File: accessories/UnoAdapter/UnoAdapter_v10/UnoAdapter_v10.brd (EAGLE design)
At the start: 71.1 x 85.7 mm, 10 parts, among them IC1 7805, X1 DC21MMX

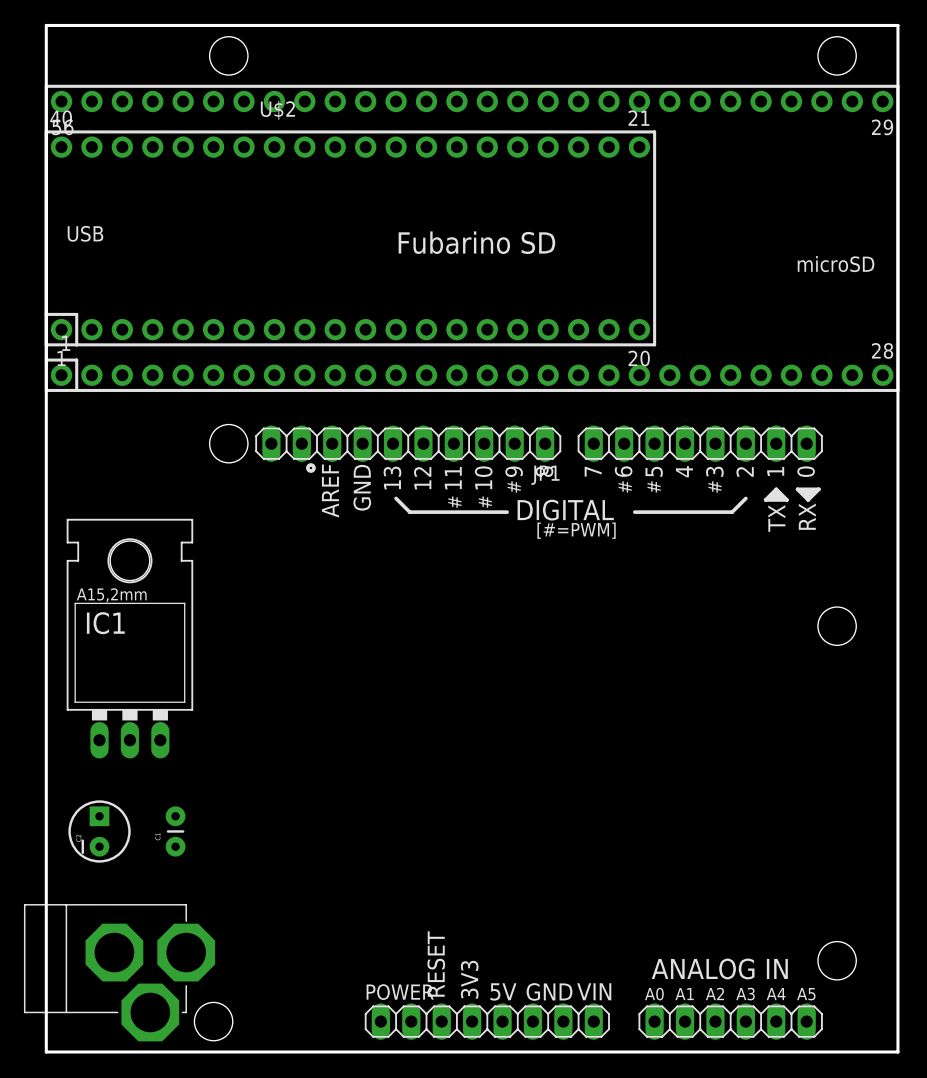
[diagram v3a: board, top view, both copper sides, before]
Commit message: Got some more work done on the board - fixed power issues, added reset/prg switches, moved Fubarinos inside Uno headers.
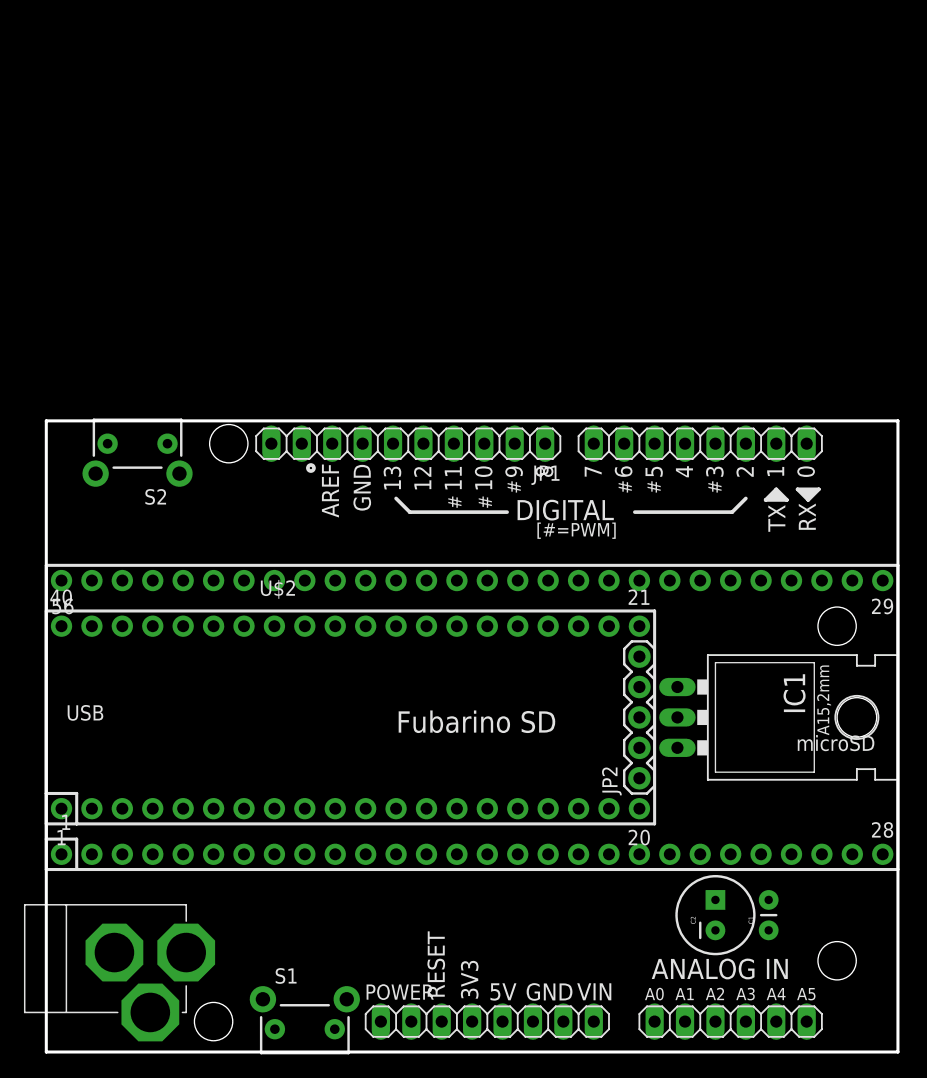
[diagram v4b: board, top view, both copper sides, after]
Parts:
- added JP2: (no value), SparkFun-Connectors:1X05
- added S1, S2: SWITCH-MOMENTARY-2SIDE_EZ, SparkFun-Electromechanical:TACTILE-PTH-SIDEEZ
- C2: value 10uF -> 100uF; device SparkFun-Capacitors:CPOL-RADIAL-10UF-25V -> SparkFun-Capacitors:CPOL-RADIAL-100UF-25V
- moved C2 51.9 mm to (55.9, 11.4)
- moved C1 50.0 mm to (60.3, 10.2)
- moved IC1 49.6 mm to (56.5, 27.9), turned to 270 degrees
- moved U$1 40.0 mm to (35.6, 27.9)
- moved U$2 40.0 mm to (25.4, 27.9)
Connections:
- removed net N$86: U$2.20
- new net N$12: JP2.4
- new net N$2: JP2.2
- new net N$3: JP2.3
- new net PRG: S2.2, U$1.27, U$2.20
- net GND: now also S1.1, S2.1
- net N$28: now also JP2.5; no longer U$1.27
- net RESET: now also JP2.1, S1.2
- net VIN: no longer U$1.56, U$2.40
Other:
- board size 71.1 x 85.7 mm -> 71.1 x 52.7 mm
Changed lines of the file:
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@@
 <layer number="144" name="Drill_legend" color="7" fill="1" visible="no" active="yes"/>
 <layer number="151" name="HeatSink" color="7" fill="1" visible="no" active="no"/>
+<layer number="199" name="Contour" color="7" fill="1" visible="yes" active="yes"/>
 <layer number="200" name="200bmp" color="1" fill="10" visible="no" active="no"/>
 <layer number="201" name="201bmp" color="2" fill="10" visible="no" active="no"/>
@@
 <board>
 <plain>
-<wire x1="0" y1="85.725" x2="71.12" y2="85.725" width="0.254" layer="20"/>
-<wire x1="71.12" y1="85.725" x2="71.12" y2="0" width="0.254" layer="20"/>
+<wire x1="0" y1="52.705" x2="71.12" y2="52.705" width="0.254" layer="20"/>
+<wire x1="71.12" y1="52.705" x2="71.12" y2="0" width="0.254" layer="20"/>
 <wire x1="71.12" y1="0" x2="0" y2="0" width="0.254" layer="20"/>
-<wire x1="0" y1="0" x2="0" y2="85.725" width="0.254" layer="20"/>
+<wire x1="0" y1="0" x2="0" y2="52.705" width="0.254" layer="20"/>
 <wire x1="60.071" y1="46.101" x2="61.849" y2="46.101" width="0.3048" layer="25"/>
 <wire x1="61.849" y1="46.101" x2="60.96" y2="46.99" width="0.3048" layer="25"/>
@@
 <hole x="15.24" y="50.8" drill="3.2"/>
 <hole x="13.97" y="2.54" drill="3.2"/>
-<hole x="15.24" y="83.185" drill="3.2"/>
-<hole x="66.04" y="83.185" drill="3.2"/>
 </plain>
 <attributes>
@@
 <attribute name="VALUE" x="11.176" y="12.319" size="1.778" layer="27" ratio="5" rot="R180"/>
 </element>
-<element name="U$1" library="SchmalzHausPublic" package="FUBARINO_SD" value="FUBARINO_SD" x="35.56" y="67.945"/>
-<element name="U$2" library="SchmalzHausPublic" package="FUBARINO_MINI" value="FUBARINO_MINI" x="25.4" y="67.945"/>
+<element name="U$1" library="SchmalzHausPublic" package="FUBARINO_SD" value="FUBARINO_SD" x="35.56" y="27.94"/>
+<element name="U$2" library="SchmalzHausPublic" package="FUBARINO_MINI" value="FUBARINO_MINI" x="25.4" y="27.94"/>
 <element name="POWER" library="pinhead" package="1X08" value="" x="36.83" y="2.54"/>
 <element name="JP1" library="pinhead" package="1X10" value="" x="30.226" y="50.8" rot="R180"/>
-<element name="IC1" library="SparkFun-PowerIC" package="78XXL" value="7805" x="6.985" y="29.845"/>
-<element name="C1" library="SparkFun-Capacitors" package="CAP-PTH-SMALL" value=".1uF" x="10.795" y="17.145" rot="R90"/>
-<element name="C2" library="SparkFun-Capacitors" package="CPOL-RADIAL-10UF-25V" value="10uF" x="4.445" y="18.415" rot="R90"/>
+<element name="IC1" library="SparkFun-PowerIC" package="78XXL" value="7805" x="56.515" y="27.94" rot="R270"/>
+<element name="C1" library="SparkFun-Capacitors" package="CAP-PTH-SMALL" value=".1uF" x="60.325" y="10.16" rot="R90"/>
+<element name="C2" library="SparkFun-Capacitors" package="CPOL-RADIAL-100UF-25V" value="100uF" x="55.88" y="11.43" rot="R90"/>
+<element name="JP2" library="SparkFun-Connectors" package="1X05" value="" x="49.53" y="22.86" rot="R90"/>
+<element name="S1" library="SparkFun-Electromechanical" package="TACTILE-PTH-SIDEEZ" value="SWITCH-MOMENTARY-2SIDE_EZ" x="21.59" y="1.905"/>
+<element name="S2" library="SparkFun-Electromechanical" package="TACTILE-PTH-SIDEEZ" value="SWITCH-MOMENTARY-2SIDE_EZ" x="7.62" y="50.8" rot="R180"/>
 </elements>
 <signals>
@@
 <contactref element="IC1" pad="OUT"/>
 <contactref element="C1" pad="1"/>
-<wire x1="1.27" y1="56.515" x2="1.27" y2="60.325" width="0" layer="19" extent="1-1"/>
-<wire x1="9.525" y1="26.035" x2="1.27" y2="56.515" width="0" layer="19" extent="1-1"/>
-<wire x1="10.795" y1="17.145" x2="9.525" y2="26.035" width="0" layer="19" extent="1-1"/>
-<wire x1="30.48" y1="2.54" x2="10.795" y2="17.145" width="0" layer="19" extent="1-1"/>
-<wire x1="38.1" y1="2.54" x2="30.48" y2="2.54" width="0" layer="19" extent="1-1"/>
+<wire x1="60.325" y1="10.16" x2="52.705" y2="25.4" width="0" layer="19" extent="1-1"/>
+<wire x1="38.1" y1="2.54" x2="60.325" y2="10.16" width="0" layer="19" extent="1-1"/>
+<wire x1="30.48" y1="2.54" x2="38.1" y2="2.54" width="0" layer="19" extent="1-1"/>
+<wire x1="1.27" y1="16.51" x2="30.48" y2="2.54" width="0" layer="19" extent="1-1"/>
+<wire x1="1.27" y1="20.32" x2="1.27" y2="16.51" width="0" layer="19" extent="1-1"/>
 </signal>
 <signal name="GND">
@@
 <contactref element="X1" pad="3"/>
 <polygon width="0.2032" layer="16" spacing="0.6096" rank="2">
-<vertex x="0" y="85.725"/>
-<vertex x="71.12" y="85.725"/>
+<vertex x="0" y="52.705"/>
+<vertex x="71.12" y="52.705"/>
 <vertex x="71.12" y="0"/>
 <vertex x="0" y="0"/>
 </polygon>
 <polygon width="0.2032" layer="1" spacing="0.6096" rank="2">
-<vertex x="0" y="85.725"/>
-<vertex x="71.12" y="85.725"/>
+<vertex x="0" y="52.705"/>
+<vertex x="71.12" y="52.705"/>
 <vertex x="71.12" y="0"/>
 <vertex x="0" y="0"/>
@@
 <contactref element="C1" pad="2"/>
 <contactref element="C2" pad="2"/>
+<contactref element="S1" pad="1"/>
+<contactref element="S2" pad="1"/>
+<wire x1="52.705" y1="27.94" x2="69.85" y2="39.37" width="0" layer="19" extent="1-1"/>
+<wire x1="60.325" y1="12.7" x2="52.705" y2="27.94" width="0" layer="19" extent="1-1"/>
+<wire x1="55.88" y1="10.16" x2="60.325" y2="12.7" width="0" layer="19" extent="1-1"/>
+<wire x1="69.85" y1="16.51" x2="60.325" y2="12.7" width="0" layer="19" extent="1-1"/>
+<wire x1="43.18" y1="2.54" x2="55.88" y2="10.16" width="0" layer="19" extent="1-1"/>
+<wire x1="40.64" y1="2.54" x2="43.18" y2="2.54" width="0" layer="19" extent="1-1"/>
+<wire x1="39.37" y1="39.37" x2="52.705" y2="27.94" width="0" layer="19" extent="1-1"/>
+<wire x1="26.416" y1="50.8" x2="39.37" y2="39.37" width="0" layer="19" extent="1-1"/>
+<wire x1="8.89" y1="35.56" x2="26.416" y2="50.8" width="0" layer="19" extent="1-1"/>
+<wire x1="3.81" y1="35.56" x2="8.89" y2="35.56" width="0" layer="19" extent="1-1"/>
+<wire x1="3.81" y1="39.37" x2="3.81" y2="35.56" width="0" layer="19" extent="1-1"/>
+<wire x1="3.81" y1="20.32" x2="3.81" y2="35.56" width="0" layer="19" extent="1-1"/>
+<wire x1="3.81" y1="16.51" x2="3.81" y2="20.32" width="0" layer="19" extent="1-1"/>
+<wire x1="5.6896" y1="8.3058" x2="3.81" y2="16.51" width="0" layer="19" extent="1-1"/>
+<wire x1="8.6868" y1="3.302" x2="5.6896" y2="8.3058" width="0" layer="19" extent="1-1"/>
+<wire x1="19.09" y1="1.905" x2="5.6896" y2="8.3058" width="0" layer="19" extent="1-1"/>
+<wire x1="10.12" y1="50.8" x2="19.09" y2="1.905" width="0" layer="19" extent="1-1"/>
 </signal>
 <signal name="AREF">
@@
 <signal name="VIN">
 <contactref element="X1" pad="2"/>
-<contactref element="U$1" pad="56"/>
-<contactref element="U$2" pad="40"/>
 <contactref element="POWER" pad="8"/>
 <contactref element="IC1" pad="IN"/>
 <contactref element="C2" pad="1"/>
-<wire x1="1.27" y1="75.565" x2="1.27" y2="79.375" width="0" layer="19" extent="1-1"/>
-<wire x1="4.445" y1="26.035" x2="1.27" y2="75.565" width="0" layer="19" extent="1-1"/>
-<wire x1="4.445" y1="19.685" x2="4.445" y2="26.035" width="0" layer="19" extent="1-1"/>
-<wire x1="11.684" y1="8.3058" x2="4.445" y2="19.685" width="0" layer="19" extent="1-1"/>
-<wire x1="45.72" y1="2.54" x2="11.684" y2="8.3058" width="0" layer="19" extent="1-1"/>
+<wire x1="55.88" y1="12.7" x2="52.705" y2="30.48" width="0" layer="19" extent="1-1"/>
+<wire x1="45.72" y1="2.54" x2="55.88" y2="12.7" width="0" layer="19" extent="1-1"/>
+<wire x1="11.684" y1="8.3058" x2="45.72" y2="2.54" width="0" layer="19" extent="1-1"/>
 </signal>
 <signal name="SCK">
@@
 <contactref element="U$2" pad="38"/>
 <contactref element="POWER" pad="4"/>
-<wire x1="6.35" y1="79.375" x2="41.91" y2="79.375" width="0" layer="19" extent="1-1"/>
-<wire x1="6.35" y1="75.565" x2="6.35" y2="79.375" width="0" layer="19" extent="1-1"/>
-<wire x1="6.35" y1="60.325" x2="6.35" y2="75.565" width="0" layer="19" extent="1-1"/>
-<wire x1="6.35" y1="56.515" x2="6.35" y2="60.325" width="0" layer="19" extent="1-1"/>
-<wire x1="35.56" y1="2.54" x2="6.35" y2="56.515" width="0" layer="19" extent="1-1"/>
+<wire x1="6.35" y1="39.37" x2="41.91" y2="39.37" width="0" layer="19" extent="1-1"/>
+<wire x1="6.35" y1="35.56" x2="6.35" y2="39.37" width="0" layer="19" extent="1-1"/>
+<wire x1="6.35" y1="20.32" x2="6.35" y2="35.56" width="0" layer="19" extent="1-1"/>
+<wire x1="6.35" y1="16.51" x2="6.35" y2="20.32" width="0" layer="19" extent="1-1"/>
+<wire x1="35.56" y1="2.54" x2="6.35" y2="16.51" width="0" layer="19" extent="1-1"/>
 </signal>
 <signal name="MISO">
@@
 <contactref element="U$1" pad="26"/>
 </signal>
-<signal name="N$28">
+<signal name="PRG">
 <contactref element="U$1" pad="27"/>
+<contactref element="U$2" pad="20"/>
+<contactref element="S2" pad="2"/>
+<wire x1="49.53" y1="20.32" x2="67.31" y2="16.51" width="0" layer="19" extent="1-1"/>
+<wire x1="5.12" y1="50.8" x2="49.53" y2="20.32" width="0" layer="19" extent="1-1"/>
 </signal>
 <signal name="N$33">
@@
 <contactref element="U$1" pad="39"/>
 <contactref element="POWER" pad="3"/>
-<wire x1="33.02" y1="2.54" x2="44.45" y2="79.375" width="0" layer="19" extent="1-1"/>
+<contactref element="JP2" pad="1"/>
+<contactref element="S1" pad="2"/>
+<wire x1="49.53" y1="22.86" x2="44.45" y2="39.37" width="0" layer="19" extent="1-1"/>
+<wire x1="33.02" y1="2.54" x2="49.53" y2="22.86" width="0" layer="19" extent="1-1"/>
+<wire x1="24.09" y1="1.905" x2="33.02" y2="2.54" width="0" layer="19" extent="1-1"/>
 </signal>
 <signal name="N$48">
@@
 <contactref element="U$2" pad="19"/>
 </signal>
-<signal name="N$86">
-<contactref element="U$2" pad="20"/>
-</signal>
 <signal name="AD4/SDA">
 <contactref element="JP1" pad="9"/>
@@
 <contactref element="JP1" pad="10"/>
 </signal>
+<signal name="N$2">
+<contactref element="JP2" pad="2"/>
+</signal>
+<signal name="N$3">
+<contactref element="JP2" pad="3"/>
+</signal>
+<signal name="N$12">
+<contactref element="JP2" pad="4"/>
+</signal>
+<signal name="N$28">
+<contactref element="JP2" pad="5"/>
+</signal>
 </signals>

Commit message: Update to UnoAdapter - still not done yet. Added Fubarino Mini v1.6 files (brought MCLR out to side pin)
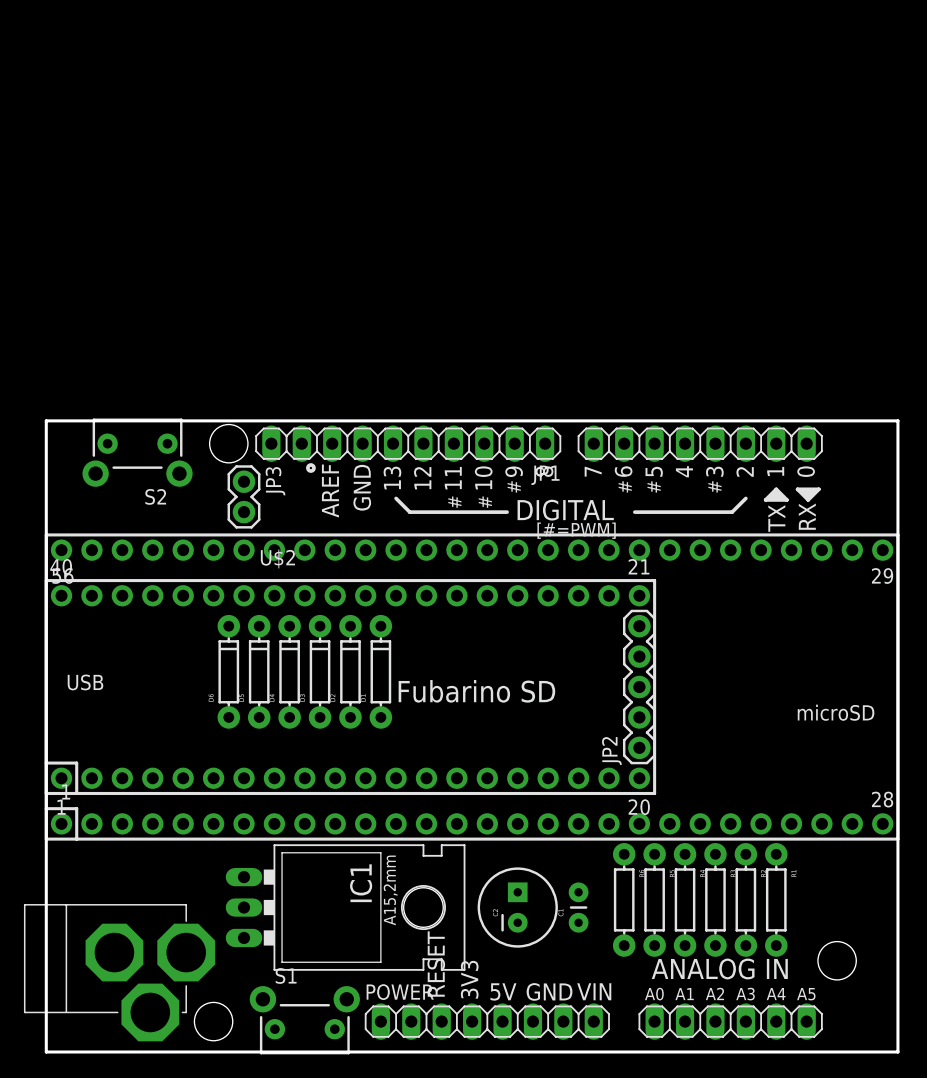
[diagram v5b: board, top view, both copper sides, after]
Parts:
- added D1, D2, D3, D4, D5, D6: (no value), SparkFun-DiscreteSemi:DIODE-1N4148
- added JP3: (no value), SparkFun-Connectors:1X02
- added R1, R2, R3, R4, R5, R6: (no value), SparkFun-Passives:AXIAL-0.3
- moved IC1 39.5 mm to (20.3, 12.1)
- moved C2 16.5 mm to (39.4, 12.1)
- moved C1 15.9 mm to (44.5, 10.8)
- moved JP2 2.54 mm to (49.5, 25.4)
- moved U$1 2.54 mm to (35.6, 30.5)
- moved U$2 2.54 mm to (25.4, 30.5)
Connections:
- removed net N$10: U$1.10
- removed net N$11: U$1.11
- removed net N$12: JP2.4
- removed net N$13: U$1.12
- removed net N$14: U$1.13
- removed net N$15: U$1.14
- removed net N$17: U$1.16
- removed net N$18: U$1.17
- removed net N$2: JP2.2
- removed net N$28: JP2.5
- removed net N$3: JP2.3
- removed net N$33: U$1.53
- removed net N$34: U$1.52
- removed net N$35: U$1.51
- removed net N$36: U$1.50
- removed net N$37: U$1.49
- removed net N$38: U$1.48
- removed net N$39: U$1.47
- removed net N$4: U$1.4
- removed net N$40: U$1.46
- removed net N$53: U$1.33
- removed net N$54: U$1.32
- removed net N$55: U$1.31
- removed net N$56: U$1.30
- removed net N$77: U$2.11
- removed net N$78: U$2.12
- removed net N$8: U$1.8
- new net $12: AD.6, R1.P$2
- new net $13: AD.5, R2.P$2
- new net $14: AD.4, R3.P$2
- new net $15: AD.3, R4.P$2
- new net $16: AD.2, R5.P$2
- new net $17: AD.1, R6.P$2
- new net M_RB0: JP2.4, U$2.11
- new net M_RB1: JP2.5, U$2.12
- new net M_RESET: JP3.2, U$2.37
- net +3V3: now also D1.C, D2.C, D3.C, D4.C, D5.C, D6.C, JP2.2, POWER.2
- net +5V: no longer POWER.2
- net AD0: now also D6.A, R6.P$1, U$1.51; no longer AD.1
- net AD1: now also D5.A, R5.P$1, U$1.50; no longer AD.2
- net AD2: now also D4.A, R4.P$1, U$1.49; no longer AD.3
- net AD3: now also D3.A, R3.P$1, U$1.48; no longer AD.4
- net AD4: now also D2.A, R2.P$1, U$1.47; no longer AD.5
- net AD4/SDA: now also U$1.52
- net AD5: now also D1.A, R1.P$1, U$1.46; no longer AD.6
- net AD5/SCL: now also U$1.53
- net GND: now also JP2.3; no longer U$2.37
- net IO0: now also U$1.16
- net IO1: now also U$1.17
- net IO2: now also U$1.8
- net IO4: now also U$1.4
- net IO5: now also U$1.14
- net IO6: now also U$1.10
- net IO7: now also U$1.11
- net IO8: now also U$1.12
- net IO9: now also U$1.13
- net MISO: now also U$1.31
- net MOSI: now also U$1.32
- net RESET: now also JP3.1
- net SCK: now also U$1.30
- net SS: now also U$1.33
